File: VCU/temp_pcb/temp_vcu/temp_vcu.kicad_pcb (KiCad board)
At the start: 2 copper layers, 33 parts, among them J1 39-30-1080, J2 39-30-1120, U2 NUCLEO-F429ZI, U3 SN65HVD233

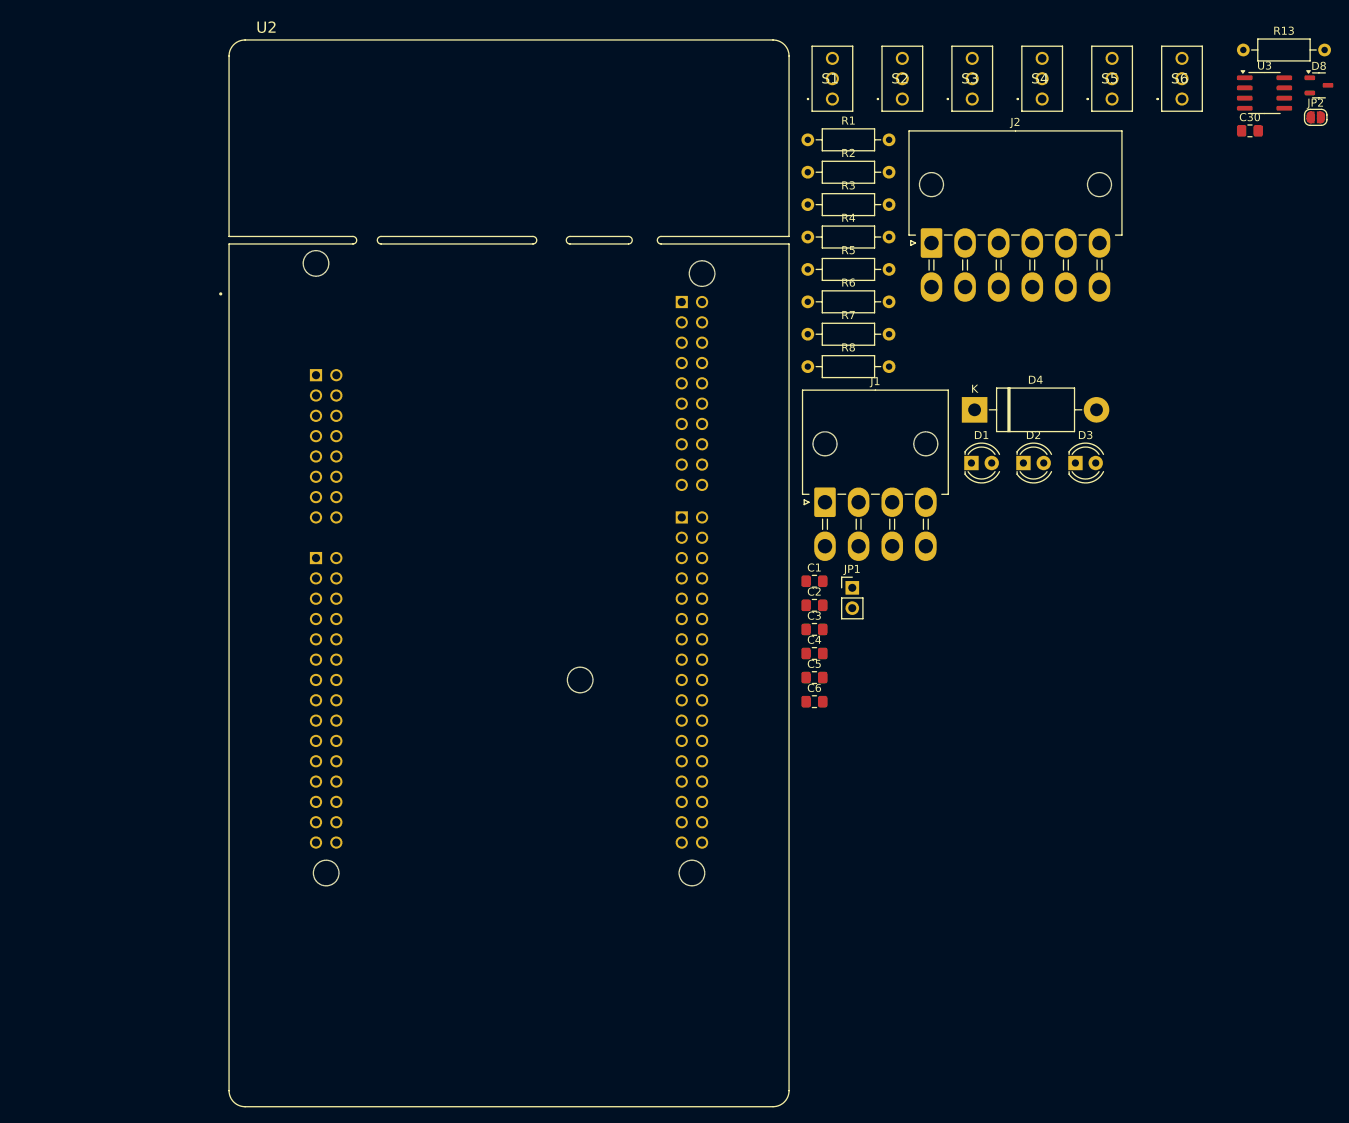
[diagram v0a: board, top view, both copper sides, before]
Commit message: Ordered version of board
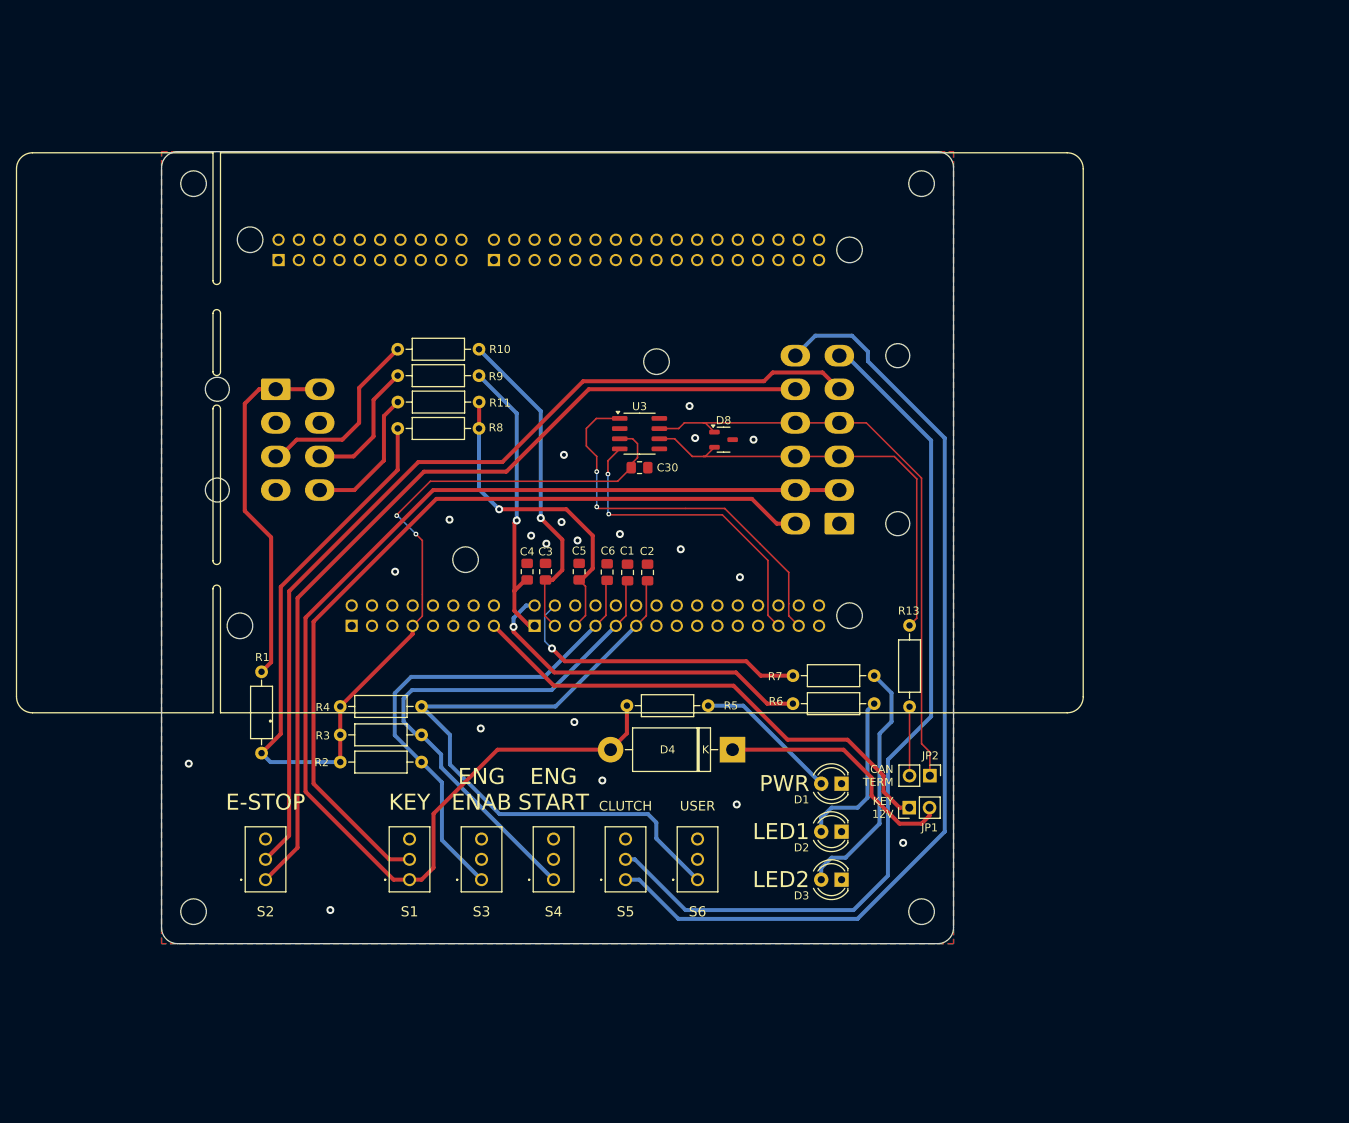
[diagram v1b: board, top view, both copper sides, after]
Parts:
- added R10: 1k, Resistor_THT:R_Axial_DIN0207_L6.3mm_D2.5mm_P10.16mm_Horizontal, F.Cu at (100.7, 73.7)
- added R11: 1k, Resistor_THT:R_Axial_DIN0207_L6.3mm_D2.5mm_P10.16mm_Horizontal, F.Cu at (90.5, 80.3)
- added R9: 1k, Resistor_THT:R_Axial_DIN0207_L6.3mm_D2.5mm_P10.16mm_Horizontal, F.Cu at (90.5, 77.0)
- added REF**: MountingHole_3.2mm_M3, MountingHole:MountingHole_3.2mm_M3, F.Cu at (65.0, 53.0)
- added REF**: MountingHole_3.2mm_M3, MountingHole:MountingHole_3.2mm_M3, F.Cu at (99.0, 100.0)
- added REF**: MountingHole_3.2mm_M3, MountingHole:MountingHole_3.2mm_M3, F.Cu at (156.0, 144.0)
- added REF**: MountingHole_3.2mm_M3, MountingHole:MountingHole_3.2mm_M3, F.Cu at (156.0, 53.0)
- added REF**: MountingHole_3.2mm_M3, MountingHole:MountingHole_3.2mm_M3, F.Cu at (65.0, 144.0)
- J1, J2: moved to B.Cu
- JP2: footprint Jumper:SolderJumper-2_P1.3mm_Open_RoundedPad1.0x1.5mm -> Connector_PinHeader_2.54mm:PinHeader_1x02_P2.54mm_Vertical
- moved S2 125.9 mm to (74.0, 140.0)
- moved S3 115.3 mm to (101.0, 140.0)
- moved S4 115.1 mm to (110.0, 140.0)
- moved S5 115.0 mm to (119.0, 140.0)
- moved S6 114.8 mm to (128.0, 140.0)
- moved S1 111.0 mm to (92.0, 140.0)
- moved JP2 95.4 mm to (157.0, 127.0), turned to -90 degrees
- moved R1 95.3 mm to (73.5, 114.0), turned to -90 degrees
- moved R13 92.1 mm to (154.5, 118.4), turned to 90 degrees
- moved U3 89.0 mm to (120.8, 84.2)
- moved R2 88.1 mm to (93.5, 125.3), turned to 180 degrees
- moved C30 87.1 mm to (120.8, 88.5), turned to 180 degrees
- moved D8 86.6 mm to (131.2, 85.0)
- moved R3 82.0 mm to (93.5, 121.9), turned to 180 degrees
- moved R4 76.0 mm to (93.5, 118.3), turned to 180 degrees
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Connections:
- net Net-(JP1-A) renamed /VIN
- C3 pad 2: /APS_2 -> /APS_2_FLT
- C4 pad 2: /APS_1 -> /APS_1_FLT
- C5 pad 2: /BRAKE_SWITCH -> /BRAKE_FLT
- J2 pad 11: /CLUTCH_GND -> /ESTOP_RETURN
- J2 pad 6: /ESTOP_RETURN -> /CLUTCH_GND
- R8 pad 1: /BRAKE_SWITCH -> /BRAKE_FLT
- U2 pad CN9_1: /APS_1 -> /APS_1_FLT
- U2 pad CN9_3: /APS_2 -> /APS_2_FLT
- U2 pad CN9_5: /BRAKE_SWITCH -> /BRAKE_FLT
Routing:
- net /KEYSWITCH_RETURN: track 0.00 -> 154.8 mm
- net +3V3: track 0.00 -> 132.6 mm, vias 0 -> 2
- net /CLUTCH_RTN: track 0.00 -> 121.4 mm
- net /ESTOP_FEED: track 0.00 -> 115.7 mm
- net /ESTOP_RETURN: track 0.00 -> 109.9 mm
- net /CLUTCH_GND: track 0.00 -> 109.7 mm
- net /KEYSWITCH_FEED: track 0.00 -> 104.0 mm
- net /USER_SWITCH: track 0.00 -> 84.0 mm
- net /CANH: track 0.00 -> 75.4 mm
- net /ENG_START: track 0.00 -> 67.3 mm
- net /ENG_ENABLE: track 0.00 -> 62.7 mm
- net /VIN: track 0.00 -> 62.5 mm
- net /CANL: track 0.00 -> 54.8 mm
- net /CAN_TX: track 0.00 -> 49.6 mm, vias 0 -> 2
- net Net-(J1-Pin_1): track 0.00 -> 45.5 mm
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- added copper zone on B.Cu, net GND
- added copper zone on F.Cu, net GND
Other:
- board outline added: 99 x 99 mm
- board text added: "CAN TERM"
- board text added: "CLUTCH"
- board text added: "E-STOP"
- board text added: "ENG ENAB"
- board text added: "ENG START"
- board text added: "KEY"
- board text added: "KEY 12V"
- board text added: "LED1"
- board text added: "LED2"
- board text added: "PWR"
- board text added: "USER"
